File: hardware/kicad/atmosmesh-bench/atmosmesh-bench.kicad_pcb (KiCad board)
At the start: 2 copper layers, 115 x 58 mm, 24 parts, among them J1 LCD1602_I2C, J2 GY-BMP280, J3 AM2302, J4 SDS011, J5 MQ135, J6 5V_IN, J7 ESP32_Harness, U1 ESP32_DevKit_V1_Socket

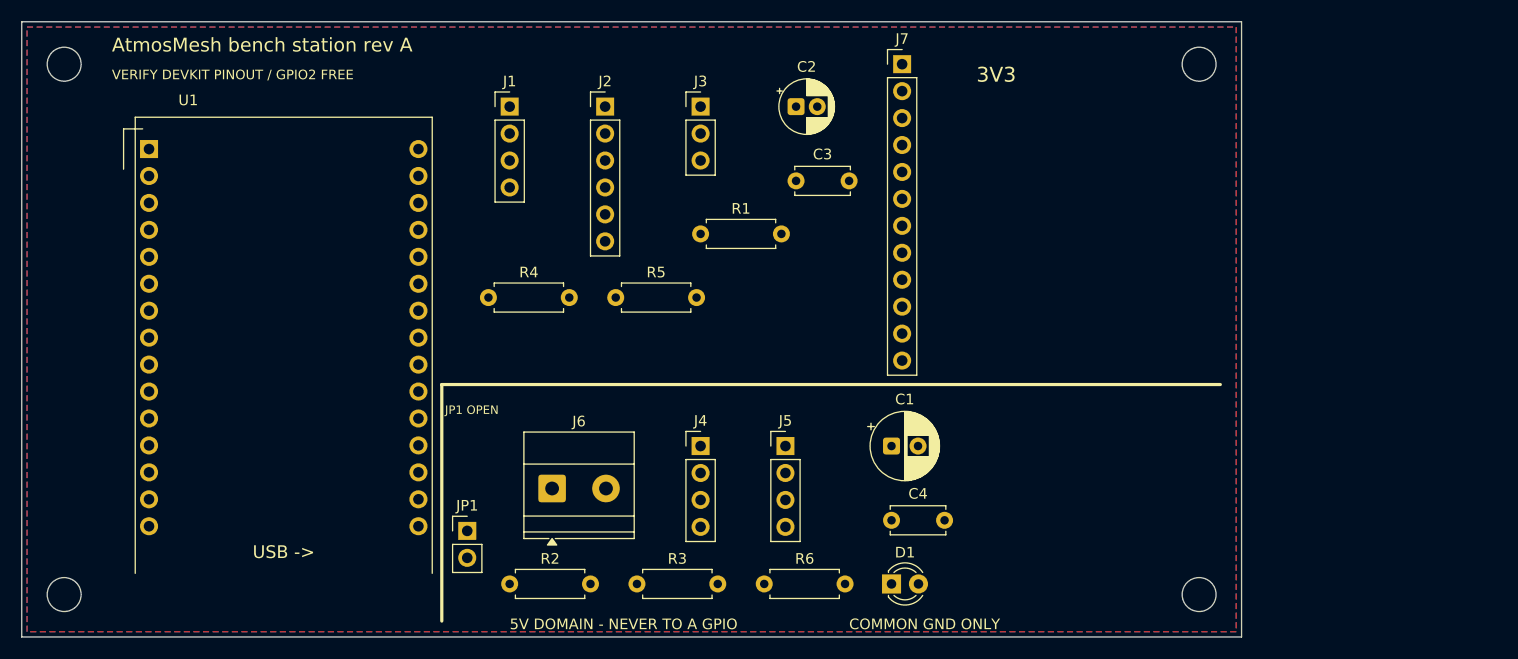
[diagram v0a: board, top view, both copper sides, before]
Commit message: :art: style(pcb): re-layout bench board into labeled 3V3/5V domain groups
- close the board outline (top edge was skewed and non-closing)
- fit GND zone to the board area (was hanging 44mm off the right edge)
- move U1 so the DevKit USB overhang fits the board, exits bottom edge
- group sensor headers, pull-ups and decoupling in a labeled 3V3 box
- group 5V input, bulk caps, LED, SDS011/MQ135 in a labeled 5V box
- add SDS011 (GPIO16/17 UART2) and MQ135 (GPIO34) lines to the
  wiring table, verified against the netlist
- DRC clean (0 violations; unconnected items expected, board is a
  trackless bench wiring guide)
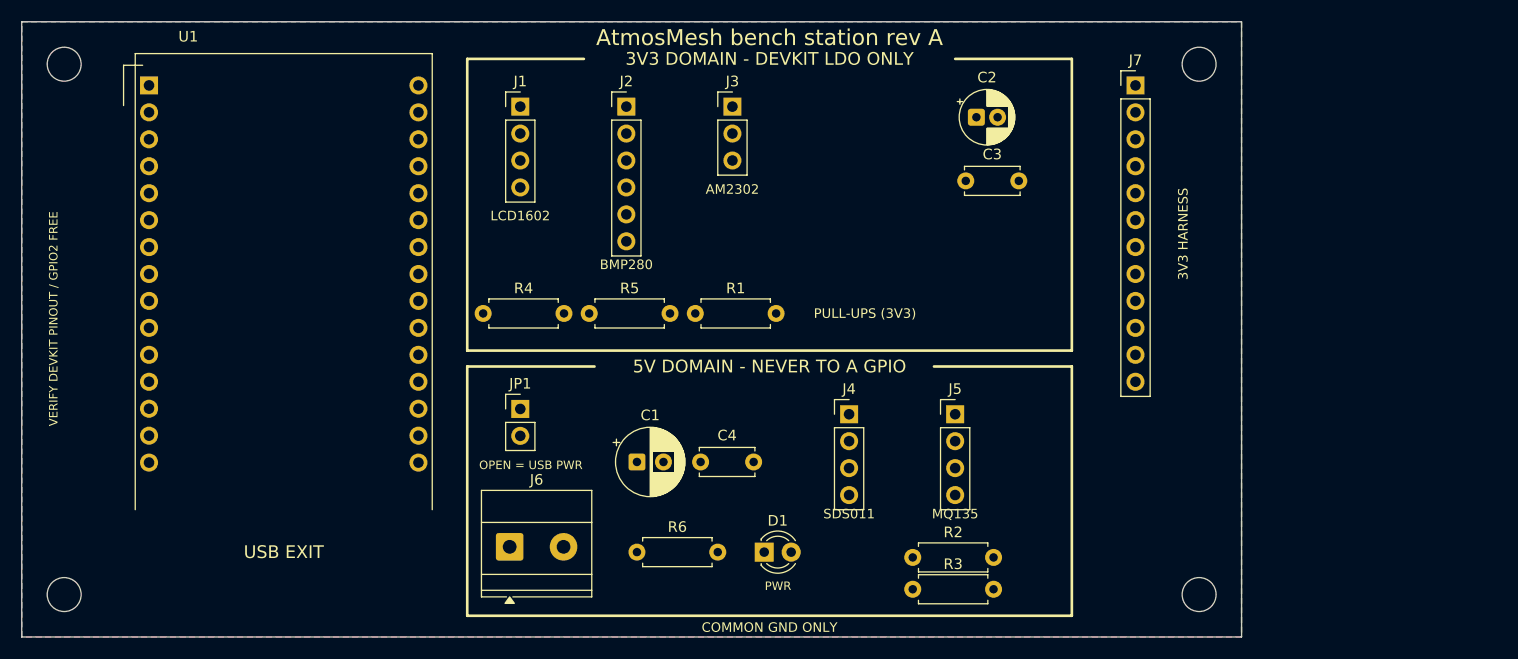
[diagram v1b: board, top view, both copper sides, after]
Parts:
- moved R2 38.1 mm to (184.0, 110.5)
- moved R3 26.0 mm to (184.0, 113.5)
- moved C1 24.0 mm to (158.0, 101.5)
- moved J7 22.1 mm to (205.0, 66.0)
- moved C4 18.8 mm to (164.0, 101.5)
- moved C2 17.0 mm to (190.0, 69.0)
- moved J5 16.3 mm to (188.0, 97.0)
- moved C3 16.0 mm to (189.0, 75.0)
- moved J4 14.3 mm to (178.0, 97.0)
- moved JP1 12.5 mm to (147.0, 96.5)
- moved D1 12.4 mm to (170.0, 110.0)
- moved R6 12.4 mm to (158.0, 110.0)
- moved R1 7.52 mm to (163.5, 87.5)
- moved J6 6.80 mm to (146.0, 109.5)
- moved U1 6.00 mm to (112.0, 66.0)
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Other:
- board text added: "3V3 DOMAIN - DEVKIT LDO ONLY"
- board text added: "3V3 HARNESS"
- board text added: "AM2302"
- board text added: "BMP280"
- board text added: "KEEPOUT: DevKit + USB cable exit"
- board text added: "LCD1602"
- board text added: "MQ135"
- board text added: "MQ135 AOUT->R2/R3 divider->GPIO34 5V"
- board text added: "OPEN = USB PWR"
- board text added: "PULL-UPS (3V3)"
- board text added: "PWR"
- board text added: "SDS011"
- board text added: "SDS011 TX->GPIO16 RX->GPIO17 (UART2) 5V"
- board text removed: "3V3"
- board text removed: "JP1 OPEN"
- board text removed: "KEEPOUT: DevKit body + USB cable exit"

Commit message: :sparkles: feat(pcb): add extras headers and route the bench board
J_BEEP/J_PIR/J_VEML, 139 mm outline, and a fully routed copper pour.
Ignore KiCad .history and restore snapshots so they stay local.
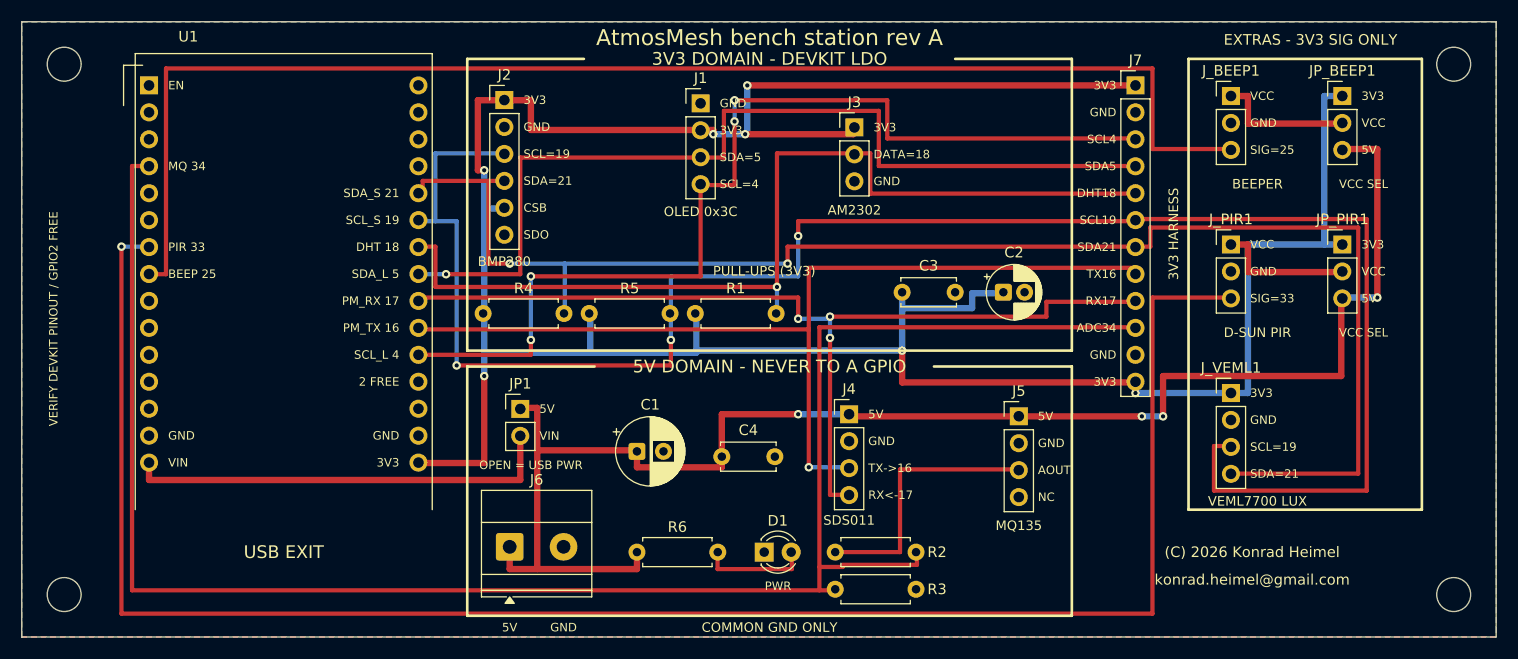
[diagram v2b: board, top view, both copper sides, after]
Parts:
- added JP_BEEP1: 3V3_5V_SEL, atmosmesh:PinHeader_1x03_P2.54mm_Vertical, F.Cu at (224.5, 67.0)
- added JP_PIR1: 3V3_5V_SEL, atmosmesh:PinHeader_1x03_P2.54mm_Vertical, F.Cu at (224.5, 81.0)
- added J_BEEP1: BEEPER, atmosmesh:PinHeader_1x03_P2.54mm_Vertical, F.Cu at (214.0, 67.0)
- added J_PIR1: D-SUN_PIR, atmosmesh:PinHeader_1x03_P2.54mm_Vertical, F.Cu at (214.0, 81.0)
- added J_VEML1: VEML7700, atmosmesh:PinHeader_1x04_P2.54mm_Vertical, F.Cu at (214.0, 95.0)
- J1: value LCD1602_I2C -> OLED_I2C
- moved H2 24.0 mm to (235.0, 64.0)
- moved H4 24.0 mm to (235.0, 114.0)
- moved J1 17.0 mm to (164.0, 67.7)
- moved C2 16.7 mm to (192.5, 85.5)
- moved C3 12.1 mm to (183.0, 85.5)
- moved J3 11.7 mm to (178.5, 70.0)
- moved J2 11.5 mm to (145.5, 67.4)
- moved R2 7.33 mm to (176.7, 110.0)
- moved R3 7.31 mm to (176.7, 113.5)
- moved J5 6.00 mm to (194.0, 97.2)
- moved C4 2.06 mm to (166.0, 101.0)
- moved C1 1.00 mm to (158.0, 100.5)
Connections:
- U1 pad 7: unconnected-(U1-GPIO33-Pad7) -> PIR_OUT
- U1 pad 8: unconnected-(U1-GPIO25-Pad8) -> BEEP_SIG
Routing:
- net +3V3: track 0.00 -> 262.9 mm, vias 0 -> 7
- net SCL_SENS: track 0.00 -> 176.1 mm, vias 0 -> 3
- net MQ_ADC: track 0.00 -> 173.3 mm
- net PIR_OUT: track 0.00 -> 171.7 mm, vias 0 -> 1
- net +5V: track 0.00 -> 147.6 mm, vias 0 -> 4
- net SDA_SENS: track 0.00 -> 142.9 mm, vias 0 -> 2
- net BEEP_SIG: track 0.00 -> 129.1 mm
- net SCL_LCD: track 0.00 -> 95.4 mm, vias 0 -> 4
- net PM_TX: track 0.00 -> 91.2 mm, vias 0 -> 1
- net DHT_DATA: track 0.00 -> 90.7 mm, vias 0 -> 1
- net PM_RX: track 0.00 -> 90.2 mm, vias 0 -> 3
- net SDA_LCD: track 0.00 -> 88.3 mm, vias 0 -> 1
- net ESP_VIN: track 0.00 -> 40.9 mm
- net MQ_AOUT: track 0.00 -> 25.4 mm
- net BEEP_VCC: track 0.00 -> 13.1 mm
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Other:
- board size 115 x 58 mm -> 139 x 58 mm
- board text added: "(C) 2026 Konrad Heimel"
- board text added: "2 FREE"
- board text added: "3V3"
- board text added: "3V3 DOMAIN - DEVKIT LDO"
- board text added: "4. JP_BEEP/JP_PIR: 5 V position only for 5 V modules."
- board text added: "5. No mains on this board."
- board text added: "5V"
- board text added: "ADC34"
- board text added: "AOUT"
- board text added: "BEEP 25"
- board text added: "BEEPER"
- board text added: "BEEPER SIG=GPIO25 (J_BEEP, VCC sel 3V3/5V)"
- board text added: "CSB"
- board text added: "D-SUN PIR"
- board text added: "DATA=18"
- board text added: "DHT 18"
- board text added: "DHT18"
- board text added: "EN"
- board text added: "EXTRAS - 3V3 SIG ONLY"
- board text added: "GND"
- board text added: "MQ 34"
- board text added: "NC"
- board text added: "OLED 0x3C"
- board text added: "OLED 0x3C SDA=GPIO5 SCL=GPIO4 VCC=3V3"
- board text added: "PIR 33"
- board text added: "PIR D-SUN SIG=GPIO33 (J_PIR, VCC sel 3V3/5V)"
- board text added: "PM_RX 17"
- board text added: "PM_TX 16"
- board text added: "RX17"
- board text added: "RX<-17"
- board text added: "SCL19"
- board text added: "SCL4"
- board text added: "SCL=19"
- board text added: "SCL=4"
- board text added: "SCL_L 4"
- board text added: "SCL_S 19"
- board text added: "SDA21"
- board text added: "SDA5"
- board text added: "SDA=21"
- board text added: "SDA=5"
- board text added: "SDA_L 5"
- board text added: "SDA_S 21"
- board text added: "SDO"
- board text added: "SIG=25"
- board text added: "SIG=33"
- board text added: "TX->16"
- board text added: "TX16"
- board text added: "VCC"
- board text added: "VCC SEL"
- board text added: "VEML7700 LUX"
- board text added: "VEML7700 SDA=GPIO21 SCL=GPIO19 shared, 0x10"
- board text added: "VIN"
- board text added: "konrad.heimel@gmail.com"
- board text removed: "3V3 DOMAIN - DEVKIT LDO ONLY"
- board text removed: "4. No mains on this board."
- board text removed: "LCD 1602 I2C SDA=GPIO5 SCL=GPIO4 VCC=3V3"
- board text removed: "LCD1602"
